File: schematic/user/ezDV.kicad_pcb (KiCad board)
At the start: 4 copper layers, 64.8 x 69.9 mm, 90 parts, among them J1 TYPE-C-31-M-04, J2 Radio_Jack, J3 User_Jack, Q1 AO3401A, Q2 AO3401A, Q3 MBT3904DW1T1, Q4 MBT3904DW1T1, Q5 MBT3904DW1T1, SW1 ESP32S3 Reset, SW2 ESP32S3 Boot Method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

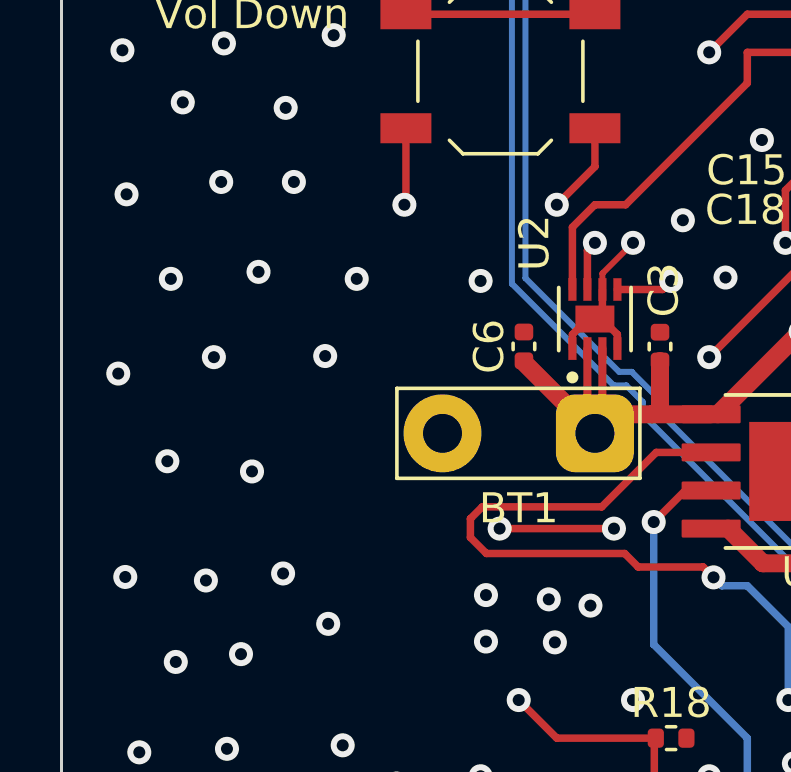
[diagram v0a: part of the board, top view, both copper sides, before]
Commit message: v0.5 board: add I2C breakout header for potential future OLED screen integration.
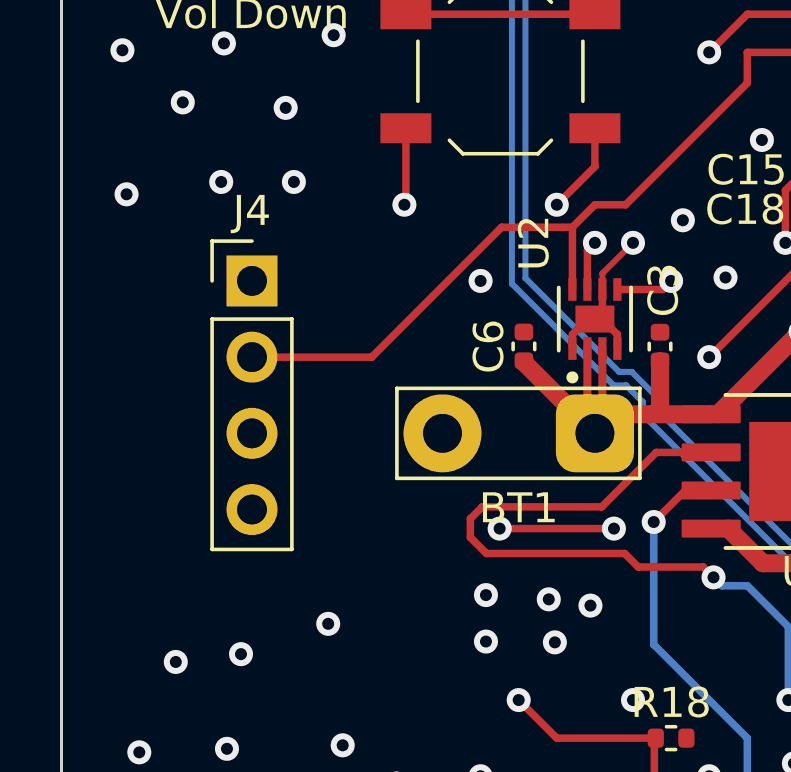
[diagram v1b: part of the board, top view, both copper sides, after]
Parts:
- added J4: I2C Breakout, Connector_PinHeader_2.54mm:PinHeader_1x04_P2.54mm_Vertical, F.Cu at (48.3, 105.4)
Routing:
- net 3.3V_PERIPH: track 45.4 -> 83.0 mm
- net GPIO45_SCL: track 44.4 -> 58.5 mm
- net GPIO47_SDA: track 43.0 -> 55.5 mm
- net GND: vias 258 -> 247

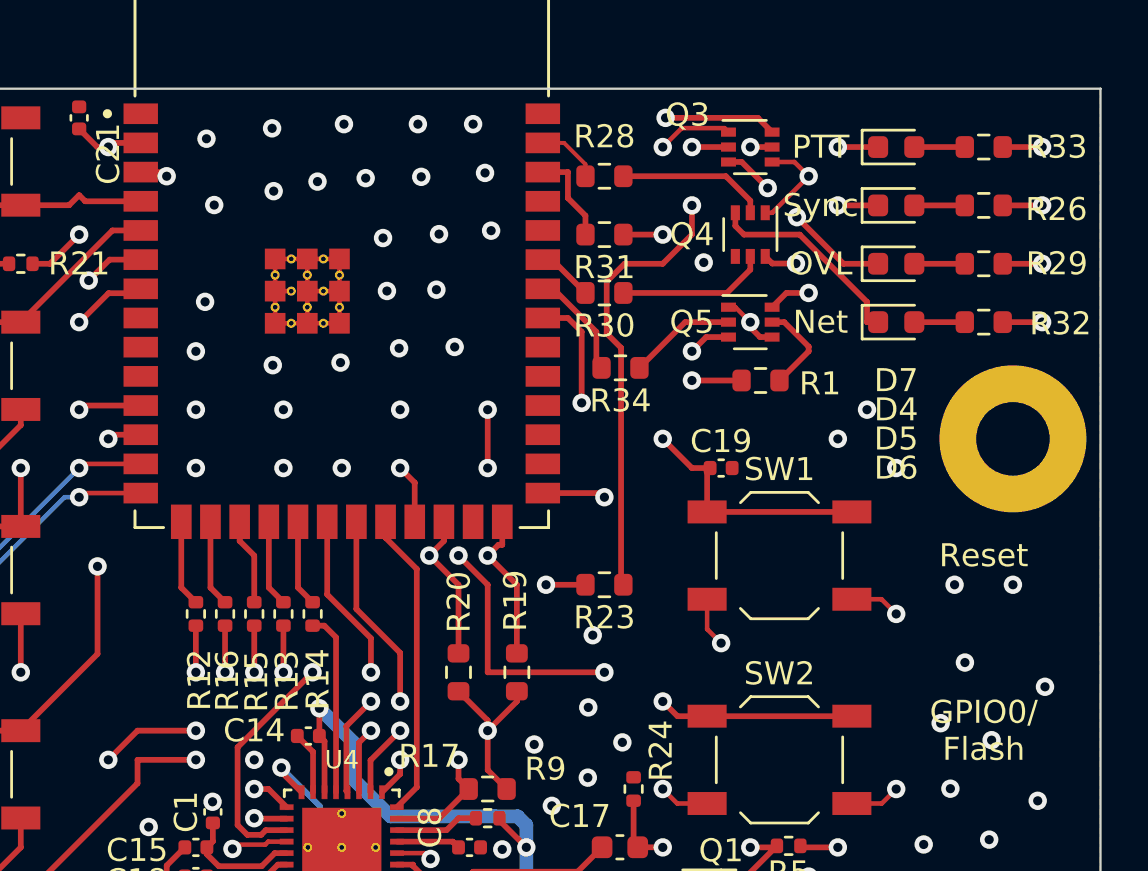
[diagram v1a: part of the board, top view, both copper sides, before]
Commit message: v0.5 board: move PERIPH_PWR GPIO to RTC to make sure it stays off when sleeping.
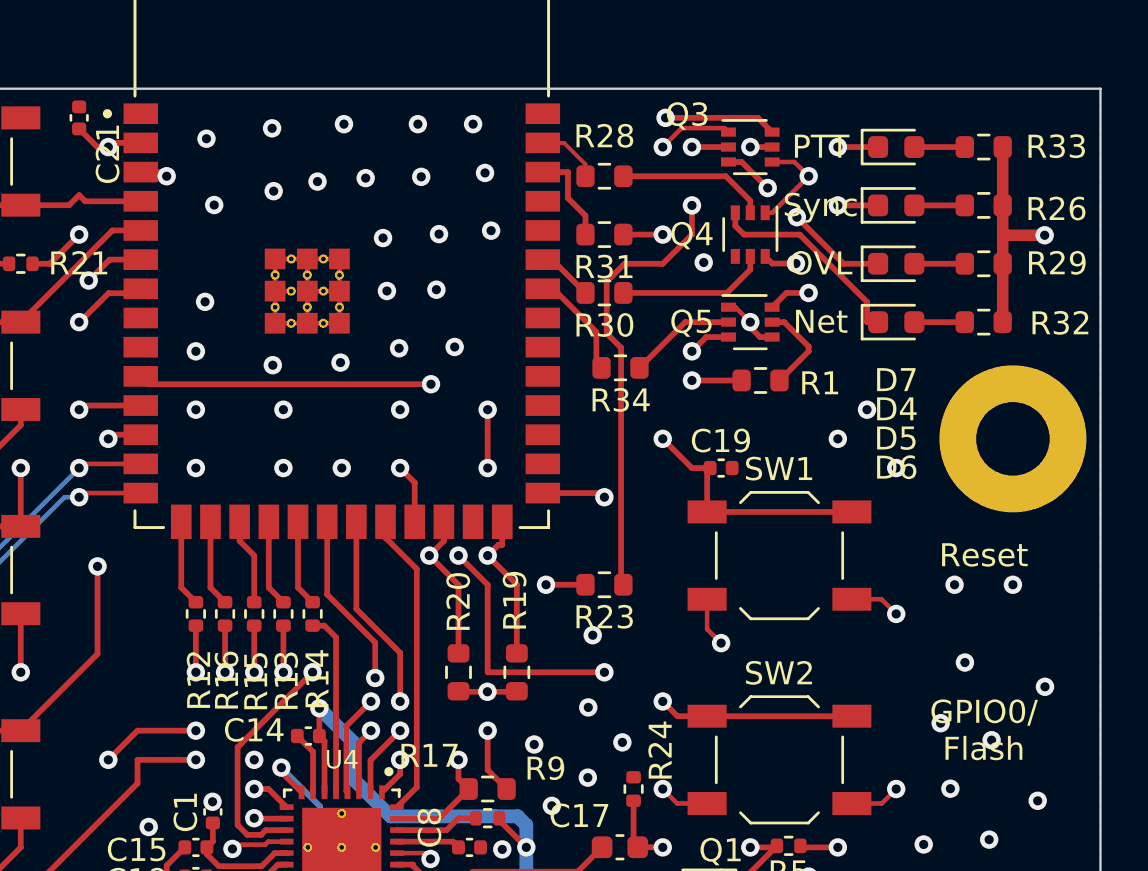
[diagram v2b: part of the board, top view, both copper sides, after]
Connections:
- R1 pad 1: GPIO40_PERIPH_PWR -> GPIO17_PERIPH_PWR
- R19 pad 1: 3.3V -> 3.3V_PERIPH
- R20 pad 1: 3.3V -> 3.3V_PERIPH
- R26 pad 2: 3.3V -> 3.3V_PERIPH
- R29 pad 2: 3.3V -> 3.3V_PERIPH
- R32 pad 1: 3.3V -> 3.3V_PERIPH
- R33 pad 2: 3.3V -> 3.3V_PERIPH
- U5 pad 10: unconnected-(U5-Pad10) -> GPIO17_PERIPH_PWR
- U5 pad 33: GPIO40_PERIPH_PWR -> unconnected-(U5-Pad33)
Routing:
- net 3.3V_PERIPH: track 83.0 -> 143.8 mm, vias 5 -> 7
- net GPIO17_PERIPH_PWR: track 0.00 -> 27.9 mm, vias 0 -> 2
- net GPIO40_PERIPH_PWR: track 12.4 -> 0.00 mm, vias 2 -> 0
- net 3.3V: track 31.5 -> 20.2 mm, vias 9 -> 5
- net GPIO12_TLV320_MFP4: track 20.3 -> 20.9 mm

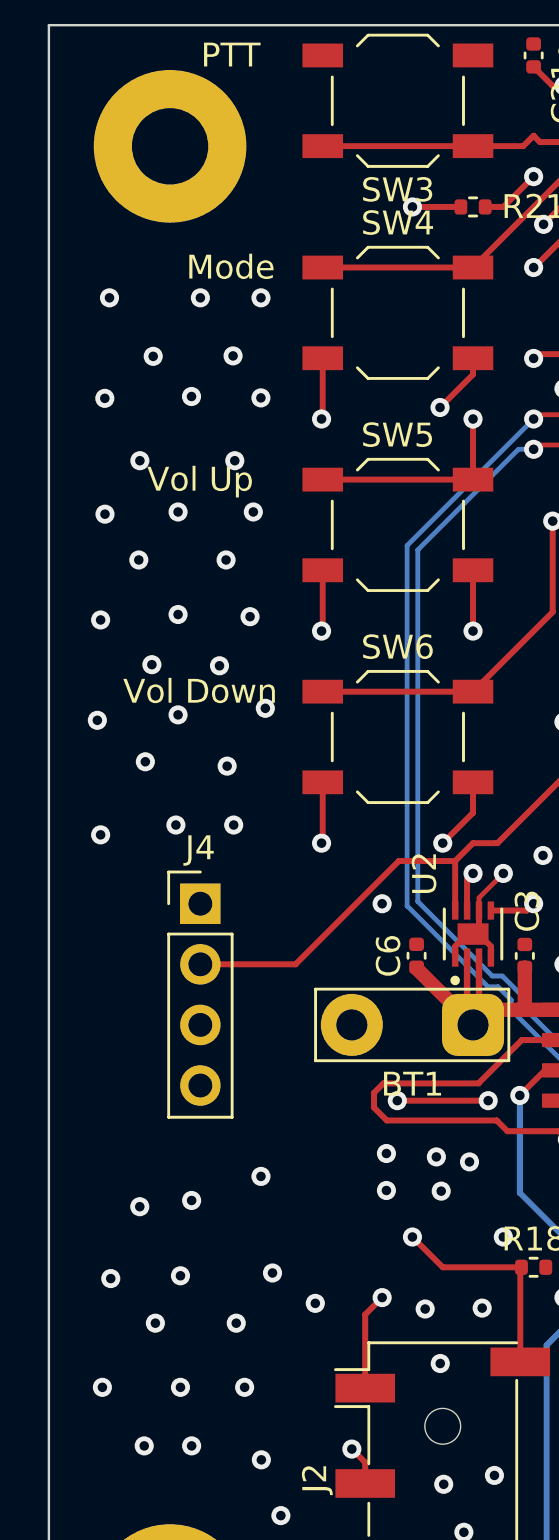
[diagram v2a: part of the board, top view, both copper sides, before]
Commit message: v0.5 board: Add PTT input breakout.
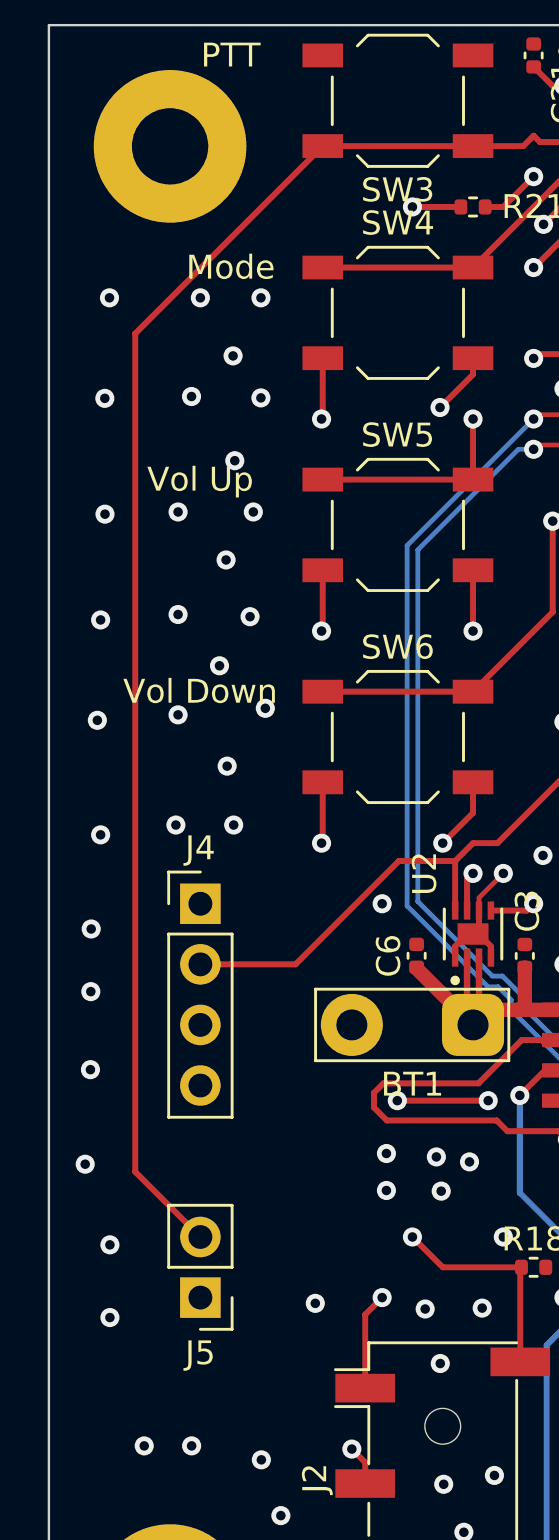
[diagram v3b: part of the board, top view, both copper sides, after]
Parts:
- added J5: PTT Breakout, Connector_PinHeader_2.54mm:PinHeader_1x02_P2.54mm_Vertical, F.Cu at (48.3, 121.9)
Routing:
- net GPIO4_PTT_IN: track 11.8 -> 61.9 mm
- net GND: vias 247 -> 237
